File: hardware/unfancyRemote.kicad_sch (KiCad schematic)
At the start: 42 parts, among them J1 Arduino Analog, J10 UART, J2 Arduino Digital, J3 HALL1, J4 HALL2, J5 PPM, J6 VIN, J7 VBAT, J8 Motor, J9 Extra analog 1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

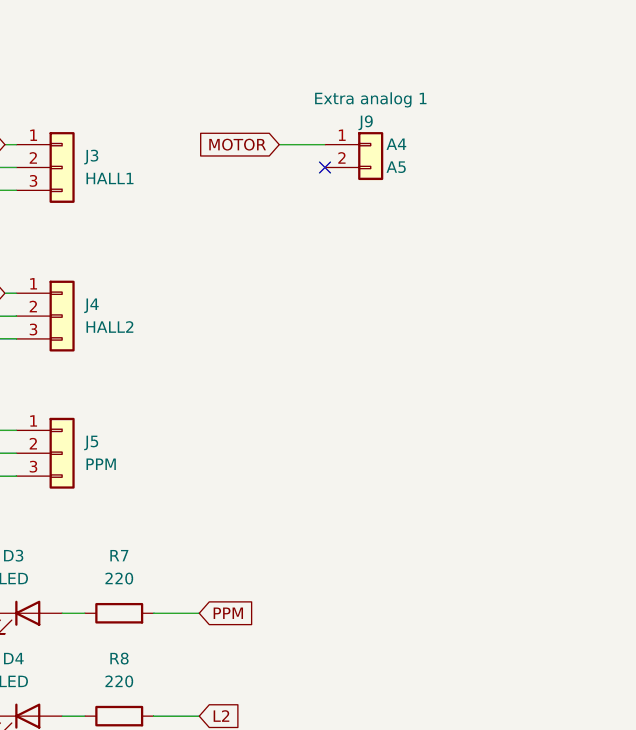
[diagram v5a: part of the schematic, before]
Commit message: Added LM4040 as ext vref
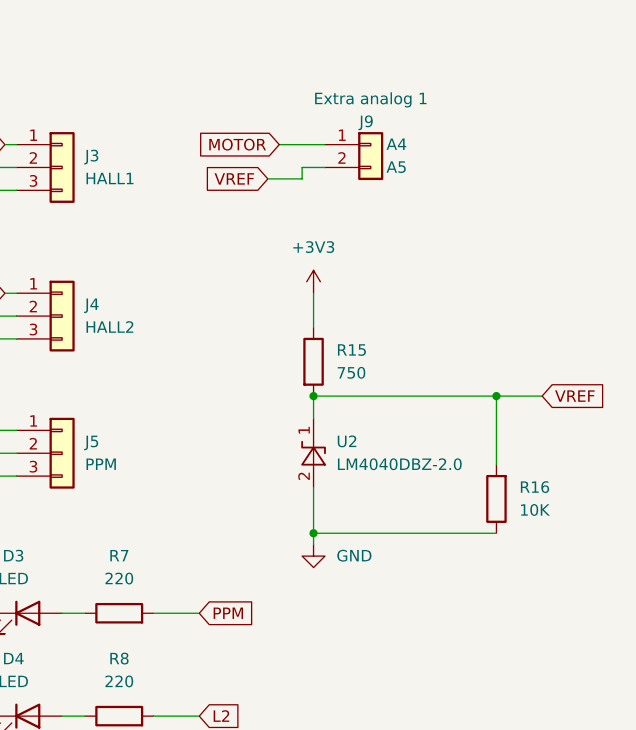
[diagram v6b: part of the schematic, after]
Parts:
- added R15: 750, Resistor_SMD:R_0603_1608Metric, symbol Device:R
- added R16: 10K, Resistor_SMD:R_0603_1608Metric, symbol Device:R
- added U2: LM4040DBZ-2.0, Package_TO_SOT_SMD:SOT-23, symbol Reference_Voltage:LM4040DBZ-2.0
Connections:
- net +3V3: now also R15.1
- net GND: now also R16.1, U2.2 (A)
- net VREF: now reaches J9.2 (A5)
- net VREF: now also R15.2, R16.2, U2.1 (K)
- no-connect marks 5 -> 4
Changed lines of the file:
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@@
   (junction (at 45.72 111.76) (diameter 0) (color 0 0 0 0)
   )
+  (junction (at 241.3 101.6) (diameter 0) (color 0 0 0 0)
+  )
   (junction (at 91.44 129.54) (diameter 0) (color 0 0 0 0)
+  )
+  (junction (at 241.3 116.84) (diameter 0) (color 0 0 0 0)
+  )
+  (junction (at 261.62 101.6) (diameter 0) (color 0 0 0 0)
   )
   (junction (at 45.72 144.78) (diameter 0) (color 0 0 0 0)
@@
   (no_connect (at 177.8 77.47))
   (no_connect (at 93.98 77.47))
-  (no_connect (at 242.57 76.2))
   (wire (pts (xy 45.72 124.46) (xy 45.72 128.27))
     (stroke (width 0) (type default) (color 0 0 0 0))
@@
     (stroke (width 0) (type default) (color 0 0 0 0))
   )
+  (wire (pts (xy 241.3 116.84) (xy 241.3 118.11))
+    (stroke (width 0) (type default) (color 0 0 0 0))
+  )
   (wire (pts (xy 118.11 97.79) (xy 118.11 85.09))
     (stroke (width 0) (type default) (color 0 0 0 0))
   )
+  (wire (pts (xy 261.62 101.6) (xy 266.7 101.6))
+    (stroke (width 0) (type default) (color 0 0 0 0))
+  )
   (wire (pts (xy 93.98 100.33) (xy 95.25 100.33))
     (stroke (width 0) (type default) (color 0 0 0 0))
@@
     (stroke (width 0) (type default) (color 0 0 0 0))
   )
+  (wire (pts (xy 240.03 77.47) (xy 236.22 77.47))
+    (stroke (width 0) (type default) (color 0 0 0 0))
+  )
   (wire (pts (xy 201.93 78.74) (xy 208.28 78.74))
     (stroke (width 0) (type default) (color 0 0 0 0))
@@
     (stroke (width 0) (type default) (color 0 0 0 0))
   )
+  (wire (pts (xy 241.3 111.76) (xy 241.3 116.84))
+    (stroke (width 0) (type default) (color 0 0 0 0))
+  )
   (wire (pts (xy 93.98 82.55) (xy 102.87 82.55))
     (stroke (width 0) (type default) (color 0 0 0 0))
@@
     (stroke (width 0) (type default) (color 0 0 0 0))
   )
+  (wire (pts (xy 261.62 109.22) (xy 261.62 101.6))
+    (stroke (width 0) (type default) (color 0 0 0 0))
+  )
   (wire (pts (xy 35.56 156.21) (xy 45.72 156.21))
     (stroke (width 0) (type default) (color 0 0 0 0))
@@
     (stroke (width 0) (type default) (color 0 0 0 0))
   )
+  (wire (pts (xy 241.3 90.17) (xy 241.3 93.98))
+    (stroke (width 0) (type default) (color 0 0 0 0))
+  )
   (wire (pts (xy 207.01 73.66) (xy 208.28 73.66))
     (stroke (width 0) (type default) (color 0 0 0 0))
@@
     (stroke (width 0) (type default) (color 0 0 0 0))
   )
+  (wire (pts (xy 261.62 101.6) (xy 241.3 101.6))
+    (stroke (width 0) (type default) (color 0 0 0 0))
+  )
   (wire (pts (xy 44.45 50.8) (xy 50.8 50.8))
     (stroke (width 0) (type default) (color 0 0 0 0))
@@
     (stroke (width 0) (type default) (color 0 0 0 0))
   )
+  (wire (pts (xy 241.3 101.6) (xy 241.3 104.14))
+    (stroke (width 0) (type default) (color 0 0 0 0))
+  )
   (wire (pts (xy 36.83 124.46) (xy 45.72 124.46))
     (stroke (width 0) (type default) (color 0 0 0 0))
@@
     (stroke (width 0) (type default) (color 0 0 0 0))
   )
+  (wire (pts (xy 240.03 76.2) (xy 240.03 77.47))
+    (stroke (width 0) (type default) (color 0 0 0 0))
+  )
   (wire (pts (xy 44.45 50.8) (xy 44.45 54.61))
     (stroke (width 0) (type default) (color 0 0 0 0))
@@
     (stroke (width 0) (type default) (color 0 0 0 0))
   )
+  (wire (pts (xy 242.57 76.2) (xy 240.03 76.2))
+    (stroke (width 0) (type default) (color 0 0 0 0))
+  )
   (wire (pts (xy 107.95 71.12) (xy 107.95 80.01))
     (stroke (width 0) (type default) (color 0 0 0 0))
@@
   )
   (wire (pts (xy 36.83 111.76) (xy 45.72 111.76))
+    (stroke (width 0) (type default) (color 0 0 0 0))
+  )
+  (wire (pts (xy 241.3 116.84) (xy 261.62 116.84))
     (stroke (width 0) (type default) (color 0 0 0 0))
   )
@@
     )
   )
+  (global_label "VREF" (shape input) (at 236.22 77.47 180) (fields_autoplaced)
+    (effects (font (size 1.27 1.27)) (justify right))
+    (property "Intersheet References" "${INTERSHEET_REFS}" (id 0) (at 229.2107 77.3906 0)
+      (effects (font (size 1.27 1.27)) (justify right) hide)
+    )
+  )
   (global_label "ON" (shape input) (at 166.37 156.21 0) (fields_autoplaced)
     (effects (font (size 1.27 1.27)) (justify left))
@@
     (effects (font (size 1.27 1.27)) (justify left))
     (property "Intersheet References" "${INTERSHEET_REFS}" (id 0) (at 111.6331 87.5506 0)
+      (effects (font (size 1.27 1.27)) (justify left) hide)
+    )
+  )
+  (global_label "VREF" (shape input) (at 266.7 101.6 0) (fields_autoplaced)
+    (effects (font (size 1.27 1.27)) (justify left))
+    (property "Intersheet References" "${INTERSHEET_REFS}" (id 0) (at 273.7093 101.5206 0)
       (effects (font (size 1.27 1.27)) (justify left) hide)
     )
@@
     (pin "2")
   )
+  (symbol (lib_id "Reference_Voltage:LM4040DBZ-2.0") (at 241.3 107.95 90) (unit 1)
+    (in_bom yes) (on_board yes) (fields_autoplaced)
+    (property "Reference" "U2" (id 0) (at 243.84 106.6799 90)
+      (effects (font (size 1.27 1.27)) (justify right))
+    )
+    (property "Value" "LM4040DBZ-2.0" (id 1) (at 243.84 109.2199 90)
+      (effects (font (size 1.27 1.27)) (justify right))
+    )
+    (property "Footprint" "Package_TO_SOT_SMD:SOT-23" (id 2) (at 246.38 107.95 0)
+      (effects (font (size 1.27 1.27) italic) hide)
+    )
+    (property "Datasheet" "http://www.ti.com/lit/ds/symlink/lm4040-n.pdf" (id 3) (at 241.3 107.95 0)
+      (effects (font (size 1.27 1.27) italic) hide)
+    )
+    (pin "1")
+    (pin "2")
+  )
   (symbol (lib_id "power:GND") (at 200.66 125.73 270) (unit 1)
     (in_bom yes) (on_board yes) (fields_autoplaced)
@@
     (pin "2")
   )
+  (symbol (lib_id "Device:R") (at 261.62 113.03 180) (unit 1)
+    (in_bom yes) (on_board yes) (fields_autoplaced)
+    (property "Reference" "R16" (id 0) (at 264.16 111.7599 0)
+      (effects (font (size 1.27 1.27)) (justify right))
+    )
+    (property "Value" "10K" (id 1) (at 264.16 114.2999 0)
+      (effects (font (size 1.27 1.27)) (justify right))
+    )
+    (property "Footprint" "Resistor_SMD:R_0603_1608Metric" (id 2) (at 263.398 113.03 90)
+      (effects (font (size 1.27 1.27)) hide)
+    )
+    (property "Datasheet" "~" (id 3) (at 261.62 113.03 0)
+      (effects (font (size 1.27 1.27)) hide)
+    )
+    (property "LCSC" "C25804" (id 4) (at 261.62 113.03 90)
+      (effects (font (size 1.27 1.27)) hide)
+    )
+    (pin "1")
+    (pin "2")
+  )
   (symbol (lib_id "Device:R") (at 115.57 156.21 90) (unit 1)
     (in_bom yes) (on_board yes) (fields_autoplaced)
@@
     (pin "2")
   )
+  (symbol (lib_id "Device:R") (at 241.3 97.79 0) (unit 1)
+    (in_bom yes) (on_board yes) (fields_autoplaced)
+    (property "Reference" "R15" (id 0) (at 243.84 96.5199 0)
+      (effects (font (size 1.27 1.27)) (justify left))
+    )
+    (property "Value" "750" (id 1) (at 243.84 99.0599 0)
+      (effects (font (size 1.27 1.27)) (justify left))
+    )
+    (property "Footprint" "Resistor_SMD:R_0603_1608Metric" (id 2) (at 239.522 97.79 90)
+      (effects (font (size 1.27 1.27)) hide)
+    )
+    (property "Datasheet" "~" (id 3) (at 241.3 97.79 0)
+      (effects (font (size 1.27 1.27)) hide)
+    )
+    (property "LCSC" "C22961" (id 4) (at 241.3 97.79 0)
+      (effects (font (size 1.27 1.27)) hide)
+    )
+    (pin "1")
+    (pin "2")
+  )
   (symbol (lib_id "power:GND") (at 124.46 80.01 270) (mirror x) (unit 1)
     (in_bom yes) (on_board yes)
@@
     )
     (property "Datasheet" "" (id 3) (at 201.93 78.74 0)
+      (effects (font (size 1.27 1.27)) hide)
+    )
+    (pin "1")
+  )
+  (symbol (lib_id "power:GND") (at 241.3 118.11 0) (unit 1)
+    (in_bom yes) (on_board yes) (fields_autoplaced)
+    (property "Reference" "#PWR?" (id 0) (at 241.3 124.46 0)
+      (effects (font (size 1.27 1.27)) hide)
+    )
+    (property "Value" "GND" (id 1) (at 243.84 119.3799 0)
+      (effects (font (size 1.27 1.27)) (justify left))
+    )
+    (property "Footprint" "" (id 2) (at 241.3 118.11 0)
+      (effects (font (size 1.27 1.27)) hide)
+    )
+    (property "Datasheet" "" (id 3) (at 241.3 118.11 0)
       (effects (font (size 1.27 1.27)) hide)
     )
@@
     (pin "1")
     (pin "2")
+  )
+  (symbol (lib_id "power:+3V3") (at 241.3 90.17 0) (unit 1)
+    (in_bom yes) (on_board yes)
+    (property "Reference" "#PWR?" (id 0) (at 241.3 93.98 0)
+      (effects (font (size 1.27 1.27)) hide)
+    )
+    (property "Value" "+3V3" (id 1) (at 241.3 85.09 0))
+    (property "Footprint" "" (id 2) (at 241.3 90.17 0)
+      (effects (font (size 1.27 1.27)) hide)
+    )
+    (property "Datasheet" "" (id 3) (at 241.3 90.17 0)
+      (effects (font (size 1.27 1.27)) hide)
+    )
+    (pin "1")
   )
   (symbol (lib_id "power:GND") (at 91.44 172.72 0) (unit 1)
@@
       (reference "#PWR0133") (unit 1) (value "GND") (footprint "")
     )
+    (path "/7af6552f-5442-466b-9530-120d4692812c"
+      (reference "#PWR?") (unit 1) (value "GND") (footprint "")
+    )
+    (path "/cc68ff3a-da7d-43ab-9911-eb2400c1a598"
+      (reference "#PWR?") (unit 1) (value "+3V3") (footprint "")
+    )
     (path "/0bb79875-05c7-4b8a-9d2d-5fca0ef83c84"
       (reference "C1") (unit 1) (value "1uF") (footprint "Capacitor_SMD:C_0603_1608Metric")
@@
       (reference "R14") (unit 1) (value "100K") (footprint "Resistor_SMD:R_0603_1608Metric")
     )
+    (path "/62efc29b-5d85-4823-a2d2-79150385cf18"
+      (reference "R15") (unit 1) (value "750") (footprint "Resistor_SMD:R_0603_1608Metric")
+    )
+    (path "/485aa1b7-c620-4b80-a621-be94212f44e6"
+      (reference "R16") (unit 1) (value "10K") (footprint "Resistor_SMD:R_0603_1608Metric")
+    )
     (path "/8e875e7b-f435-48fe-904e-cd96af2470b5"
       (reference "SW1") (unit 1) (value "SW_Push") (footprint "Button_Switch_SMD:SW_SPST_PTS645")
@@
       (reference "U1") (unit 1) (value "E28-2G4M12S") (footprint "unfancyRemote_components:E28-2G4M12S")
     )
-  )
+    (path "/388e0b2e-f12c-440a-bef0-a4828b58b69d"
+      (reference "U2") (unit 1) (value "LM4040DBZ-2.0") (footprint "Package_TO_SOT_SMD:SOT-23")
+    )
+  )
